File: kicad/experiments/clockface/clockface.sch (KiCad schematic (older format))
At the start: 11 parts, among them P1 CONN_01X05, U1 TOUCH_PAD_13, U2 MTCH6102_SSOP

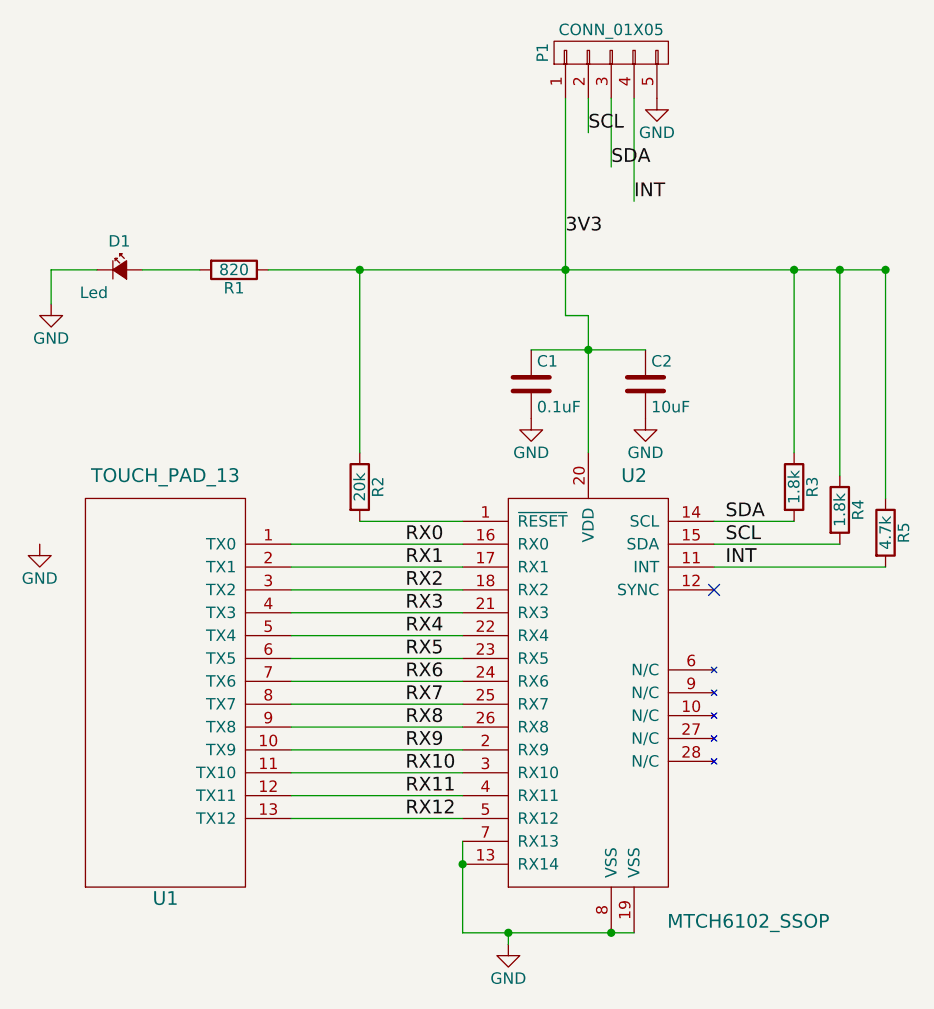
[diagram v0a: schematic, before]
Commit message: Corrected SDA & SCL labels
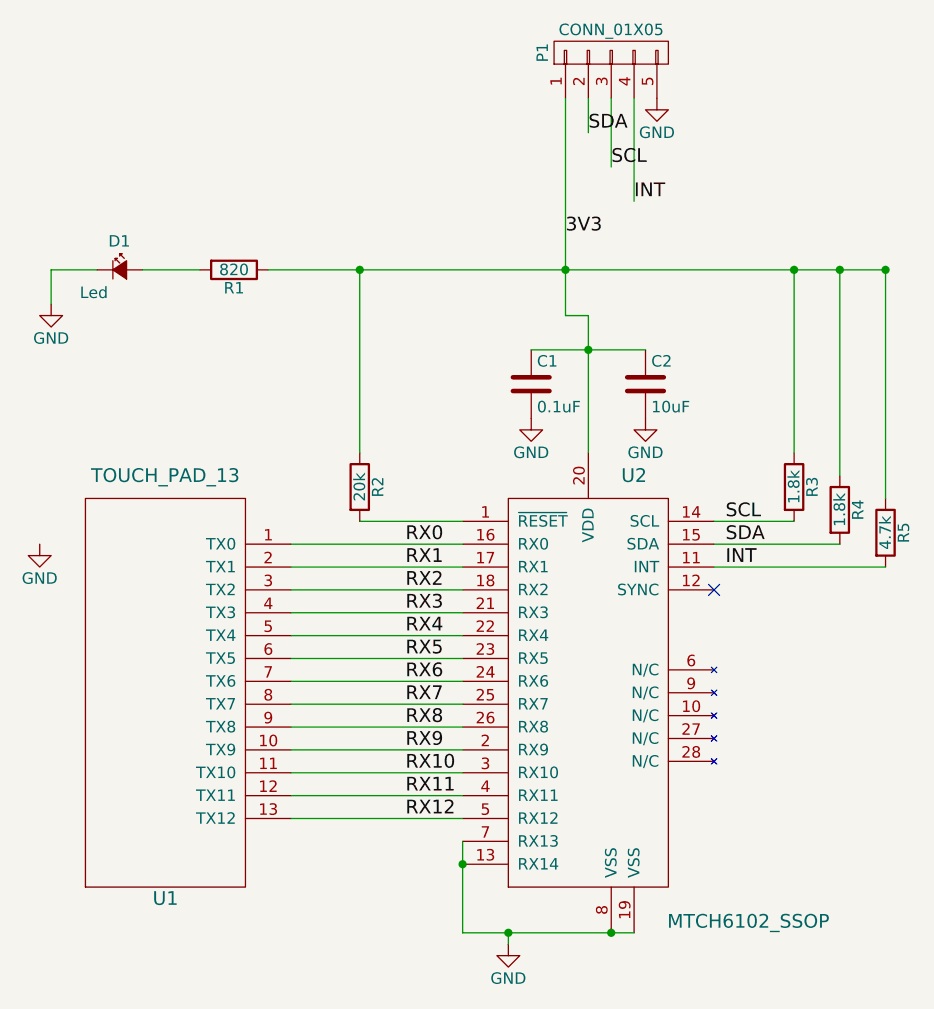
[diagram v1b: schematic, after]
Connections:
- net SCL: now also P1.3 (P3), R3.2, U2.14 (SCL); no longer P1.2 (P2), R4.2, U2.15 (SDA)
- net SDA: now also P1.2 (P2), R4.2, U2.15 (SDA); no longer P1.3 (P3), R3.2, U2.14 (SCL)
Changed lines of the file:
@@
 	1    0    0    -1
 $EndComp
+Text Label 6700 3600 0    60   ~ 0
+SDA
 Text Label 6700 3500 0    60   ~ 0
-SDA
-Text Label 6700 3600 0    60   ~ 0
 SCL
 Text Label 6700 3700 0    60   ~ 0
@@
 	0    -1   -1   0
 $EndComp
+Text Label 6100 1800 0    60   ~ 0
+SDA
 Text Label 6200 1950 0    60   ~ 0
-SDA
-Text Label 6100 1800 0    60   ~ 0
 SCL
 Text Label 6300 2100 0    60   ~ 0
